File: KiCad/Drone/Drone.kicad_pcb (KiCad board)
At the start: 2 copper layers, 91.4 x 57.1 mm, 22 parts, among them J1 ESC, J10 to ESC Power, J11 Conn_01x02_Female, J2 BATTRY, J3 ESP32_LEFT, J4 Raspberry Pi, J5 ESP32_RIGHT, J6 DPS310_LEFT, J7 US-015, J8 MPU9250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

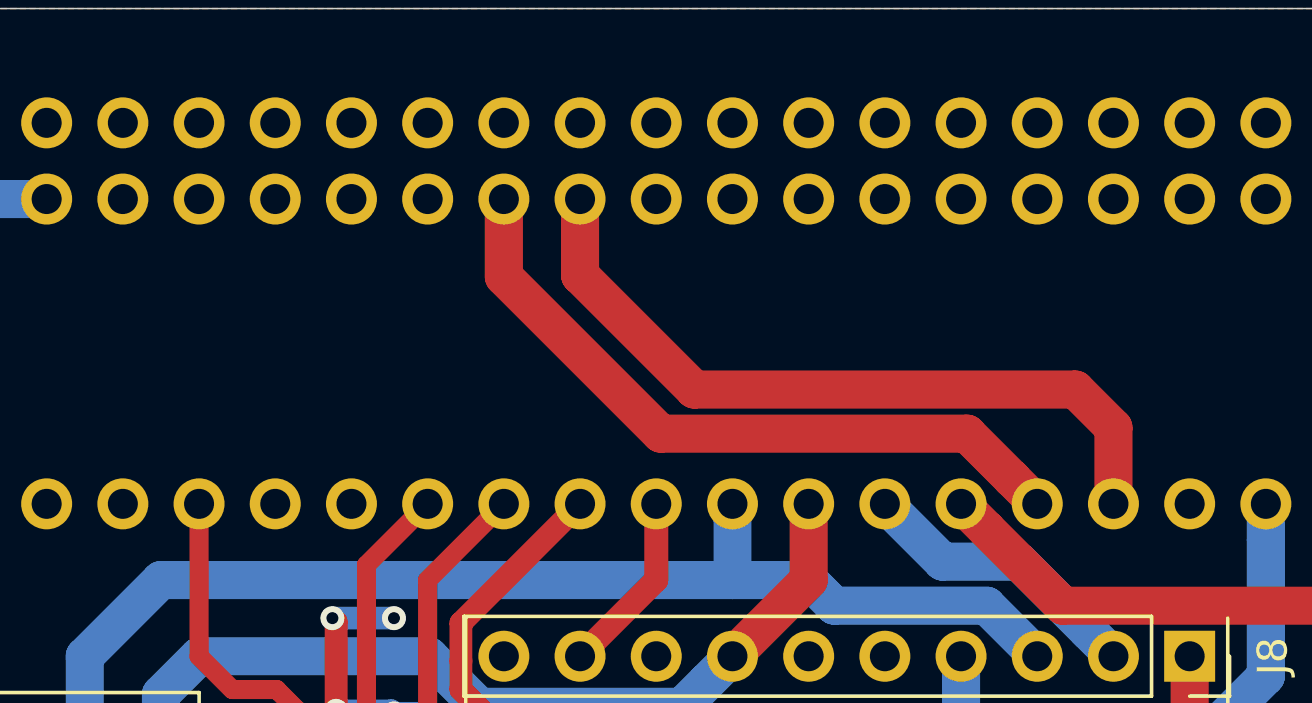
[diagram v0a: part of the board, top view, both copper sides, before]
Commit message: [MOD]UARTピンの変更
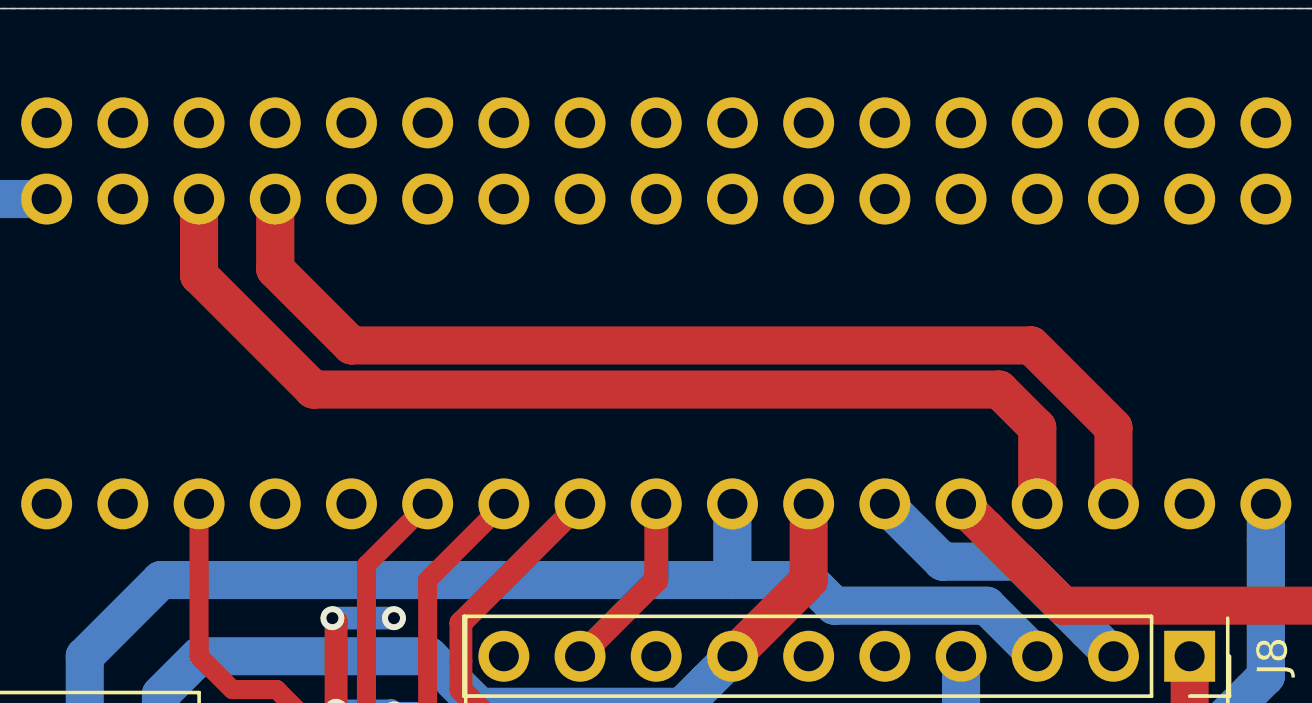
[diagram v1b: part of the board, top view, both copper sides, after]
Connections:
- J5 pad 4: PI_PIGPIO_RX -> PI_UART_RX
- J5 pad 5: PI_PIGPIO_TX -> PI_UART_TX
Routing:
- net PI_UART_TX: track 0.00 -> 35.1 mm
- net PI_UART_RX: track 0.00 -> 35.0 mm
- net PI_PIGPIO_RX: track 25.0 -> 0.00 mm
- net PI_PIGPIO_TX: track 23.5 -> 0.00 mm
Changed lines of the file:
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@@
   (page A4)
   (layers
-    (0 F.Cu signal hide)
-    (31 B.Cu signal hide)
+    (0 F.Cu signal)
+    (31 B.Cu signal)
     (32 B.Adhes user)
     (33 F.Adhes user hide)
@@
   )
   (setup
-    (last_trace_width 0.25)
+    (last_trace_width 1.27)
     (user_trace_width 0.254)
     (user_trace_width 0.508)
@@
       (net 8 GPIO22))
     (pad 4 thru_hole oval (at 0 -7.62 90) (size 1.7 1.7) (drill 1) (layers *.Cu *.Mask)
-      (net 58 PI_PIGPIO_RX))
+      (net 23 PI_UART_RX))
     (pad 5 thru_hole oval (at 0 -10.16 90) (size 1.7 1.7) (drill 1) (layers *.Cu *.Mask)
-      (net 57 PI_PIGPIO_TX))
+      (net 22 PI_UART_TX))
     (pad 6 thru_hole oval (at 0 -12.7 90) (size 1.7 1.7) (drill 1) (layers *.Cu *.Mask)
       (net 7 GPIO21))
@@
   (segment (start 146.05 106.27309) (end 143.841988 108.481102) (width 1.27) (layer B.Cu) (net 21))
   (segment (start 146.05 102.87) (end 146.05 106.27309) (width 1.27) (layer B.Cu) (net 21))
+  (segment (start 109.22 81.28) (end 109.22 78.74) (width 1.27) (layer F.Cu) (net 22))
+  (segment (start 113.03 85.09) (end 109.22 81.28) (width 1.27) (layer F.Cu) (net 22))
+  (segment (start 135.89 85.09) (end 113.03 85.09) (width 1.27) (layer F.Cu) (net 22))
+  (segment (start 137.16 86.36) (end 135.89 85.09) (width 1.27) (layer F.Cu) (net 22))
+  (segment (start 137.16 88.9) (end 137.16 86.36) (width 1.27) (layer F.Cu) (net 22))
+  (segment (start 111.76 78.74) (end 111.76 81.07999) (width 1.27) (layer F.Cu) (net 23))
+  (segment (start 114.3 83.61999) (end 136.95999 83.61999) (width 1.27) (layer F.Cu) (net 23))
+  (segment (start 111.76 81.07999) (end 114.3 83.61999) (width 1.27) (layer F.Cu) (net 23))
+  (segment (start 139.7 86.36) (end 139.7 88.9) (width 1.27) (layer F.Cu) (net 23))
+  (segment (start 136.95999 83.61999) (end 139.7 86.36) (width 1.27) (layer F.Cu) (net 23))
   (segment (start 110.328999 95.088999) (end 111.804801 95.088999) (width 0.635) (layer F.Cu) (net 26))
   (segment (start 109.22 93.98) (end 110.328999 95.088999) (width 0.635) (layer F.Cu) (net 26))
@@
   (segment (start 104.740001 98.390001) (end 132.749999 98.390001) (width 1.27) (layer B.Cu) (net 52))
   (segment (start 102.87 96.52) (end 104.740001 98.390001) (width 1.27) (layer B.Cu) (net 52))
-  (segment (start 134.820009 86.560009) (end 136.310001 88.050001) (width 1.27) (layer F.Cu) (net 57))
-  (segment (start 119.38 81.326198) (end 124.613811 86.560009) (width 1.27) (layer F.Cu) (net 57))
-  (segment (start 136.310001 88.050001) (end 137.16 88.9) (width 1.27) (layer F.Cu) (net 57))
-  (segment (start 124.613811 86.560009) (end 134.820009 86.560009) (width 1.27) (layer F.Cu) (net 57))
-  (segment (start 119.38 78.74) (end 119.38 81.326198) (width 1.27) (layer F.Cu) (net 57))
-  (segment (start 138.43 85.09) (end 139.7 86.36) (width 1.27) (layer F.Cu) (net 58))
-  (segment (start 139.7 86.36) (end 139.7 88.9) (width 1.27) (layer F.Cu) (net 58))
-  (segment (start 125.73 85.09) (end 138.43 85.09) (width 1.27) (layer F.Cu) (net 58))
-  (segment (start 121.92 78.74) (end 121.92 81.28) (width 1.27) (layer F.Cu) (net 58))
-  (segment (start 121.92 81.28) (end 125.73 85.09) (width 1.27) (layer F.Cu) (net 58))
   (segment (start 135.474999 92.294999) (end 130.394999 92.294999) (width 1.27) (layer B.Cu) (net 69))
   (segment (start 137.16 93.98) (end 135.474999 92.294999) (width 1.27) (layer B.Cu) (net 69))

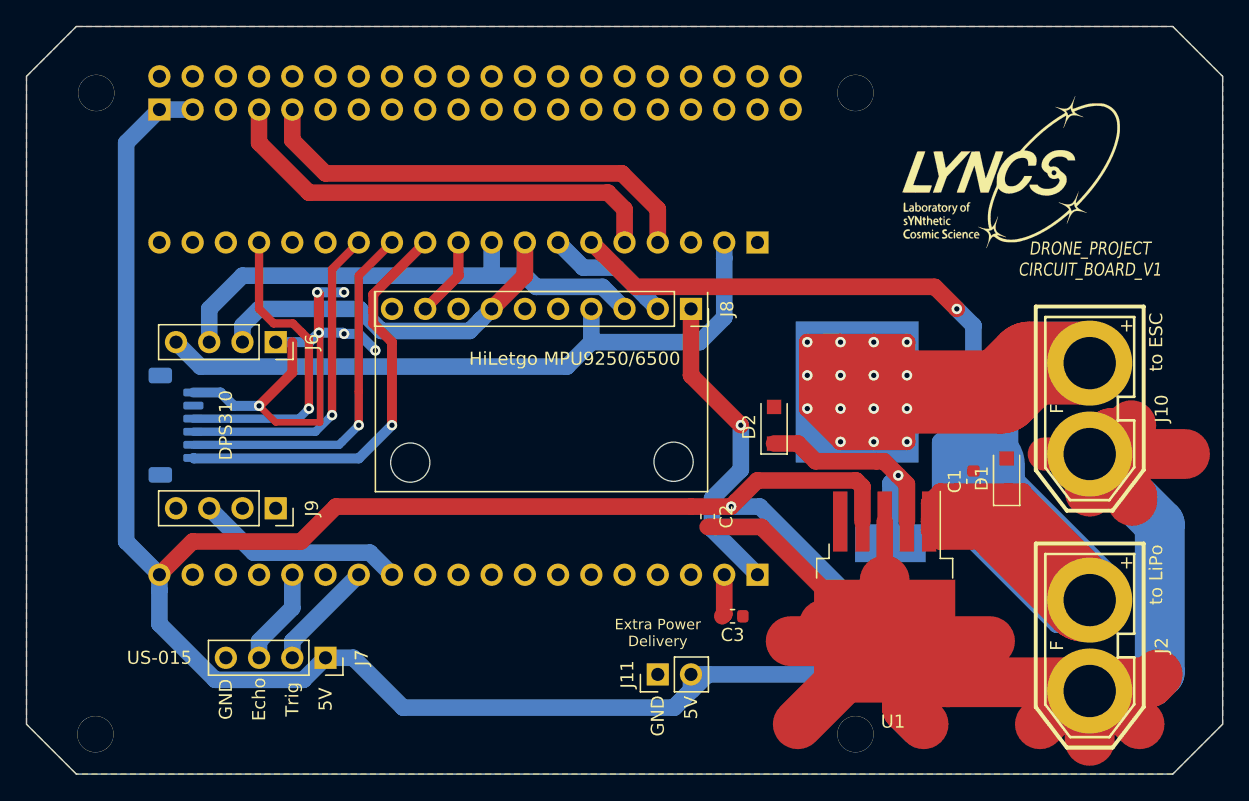
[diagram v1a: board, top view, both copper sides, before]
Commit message: [MOD]:bug:MOSFET周りの修正
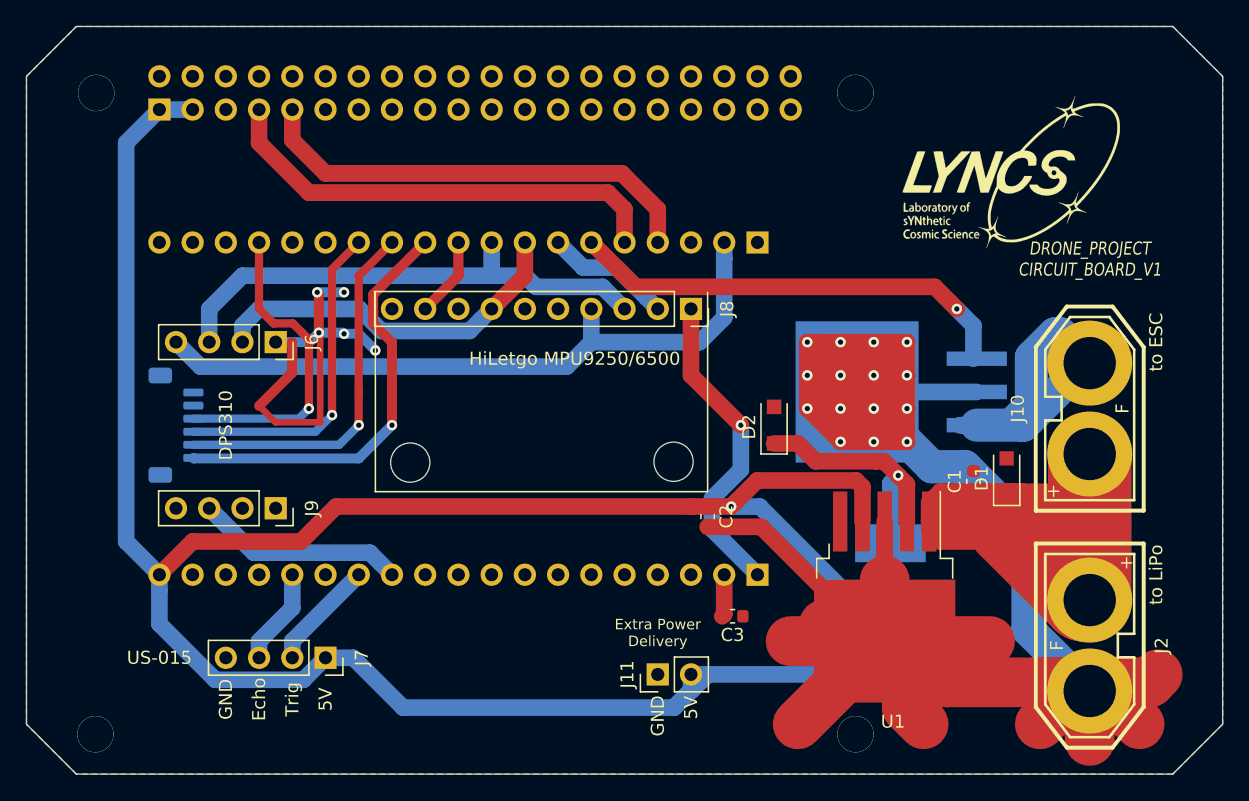
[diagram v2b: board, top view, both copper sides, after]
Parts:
- turned J10 to 90 degrees
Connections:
- J1 pad 1: GND -> Net-(J1-Pad1)
- J10 pad 1: GND -> ESC_GND
- J10 pad 2: ESC_VIN -> BAT
- U2 pad 2: ESC_VIN -> GND
- U2 pad 3: BAT -> ESC_GND
- U2 pad 4: ESC_VIN -> GND
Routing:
- net ESC_VIN: track 169.5 -> 0.00 mm, vias 15 -> 0
- net GND: track 199.3 -> 307.8 mm, vias 6 -> 20
- net BAT: track 102.6 -> 73.1 mm
- net ESC_GND: track 0.00 -> 23.5 mm
- net Net-(D2-Pad1): track 20.7 -> 19.7 mm

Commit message: :recycle:銅線を太くしたり
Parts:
- removed C2: 22u, Capacitor_SMD:C_0603_1608Metric
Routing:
- net 3V3: track 24.3 -> 19.3 mm
- net 5V: track 189.7 -> 193.9 mm

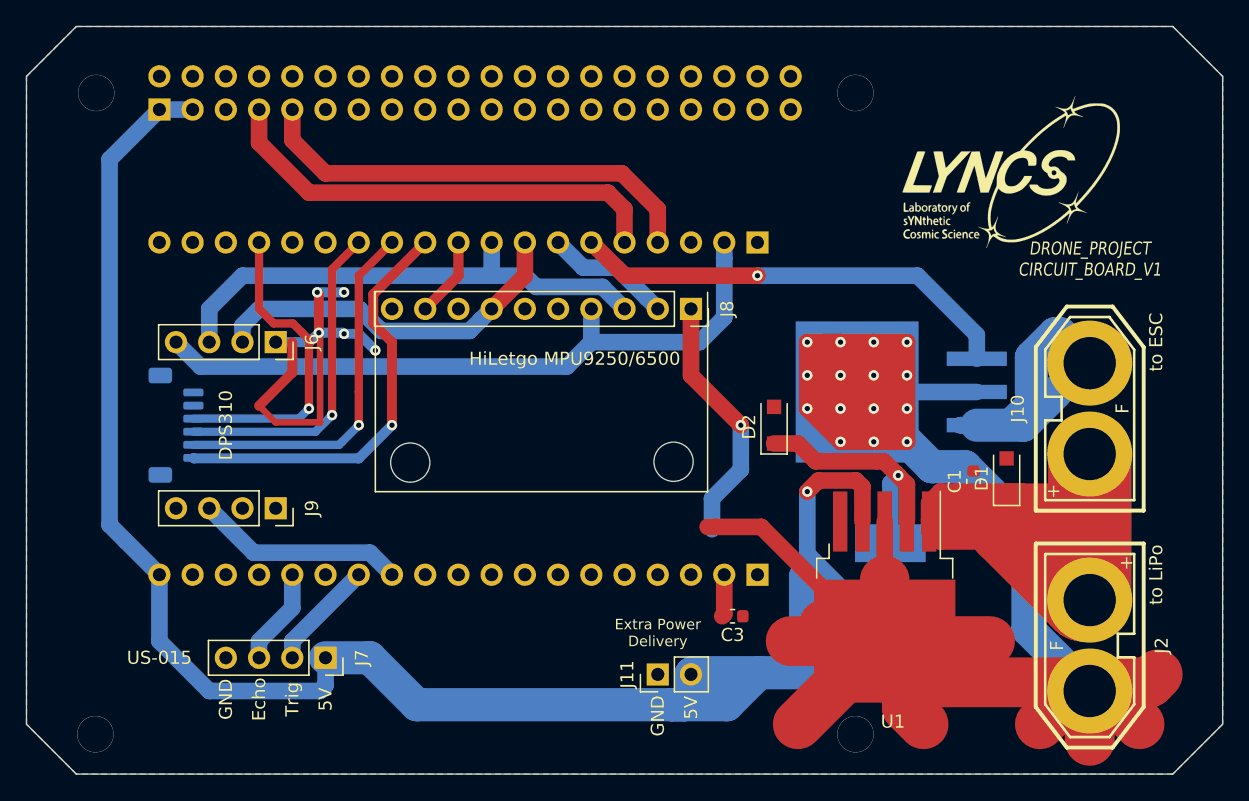
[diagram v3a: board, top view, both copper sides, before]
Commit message: :bug:回路の変更 (#23)
* :bug:ESCの位置と回路の変更

* :recycle:微調整

* :recycle:ESCの位置を変更
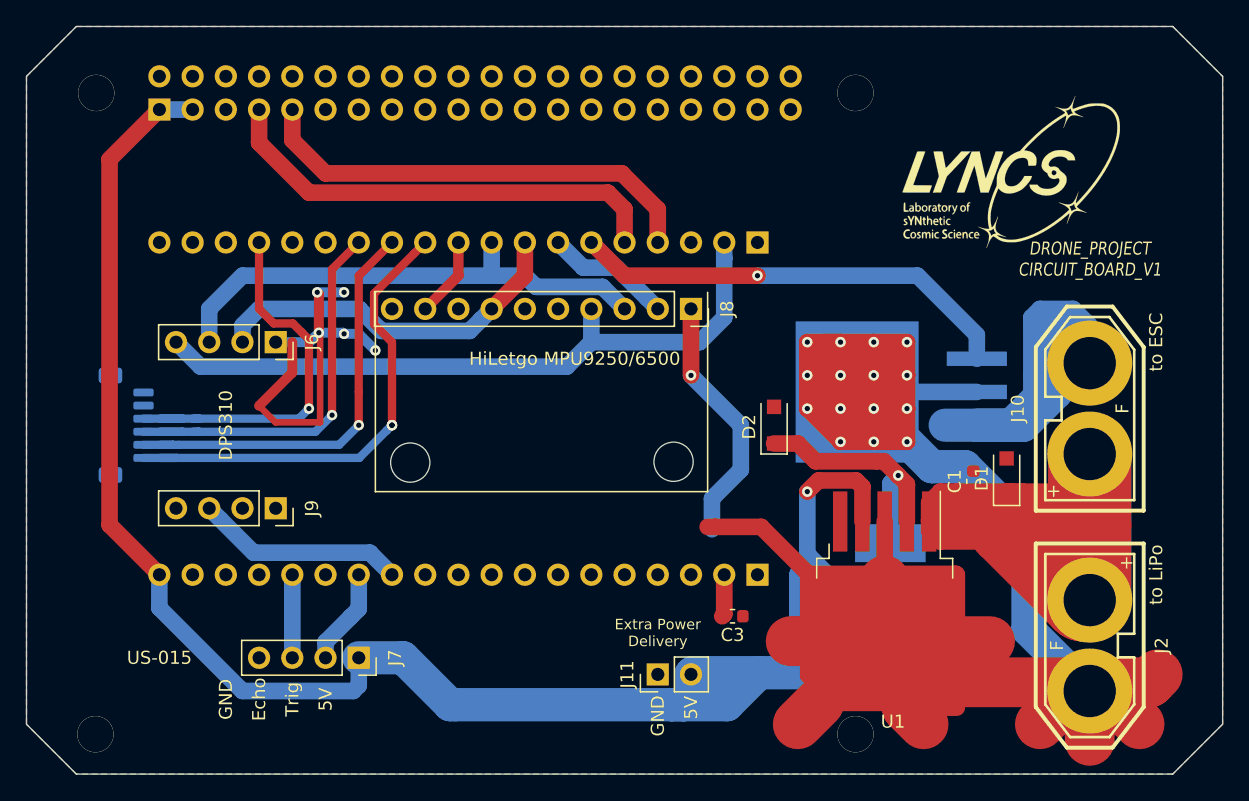
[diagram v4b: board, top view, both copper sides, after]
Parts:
- moved J1 3.81 mm to (99.1, 102.9)
- moved J7 2.54 mm to (116.8, 120.7)
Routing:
- net GND: track 307.8 -> 368.0 mm
- net ESC_GND: track 23.5 -> 46.1 mm
- net 5V: track 193.9 -> 202.0 mm
- net GPIO4: track 25.2 -> 31.1 mm
- net GPIO15: track 24.3 -> 30.3 mm
- net GPIO17: track 32.5 -> 37.4 mm, vias 1 -> 2
- net GPIO16: track 28.3 -> 33.1 mm
- net Echo: track 7.40 -> 6.35 mm
- net GPIO12: track 8.45 -> 7.40 mm
